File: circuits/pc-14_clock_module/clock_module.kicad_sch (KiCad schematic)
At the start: 7 parts, among them U1 74HCT74, U2 4011

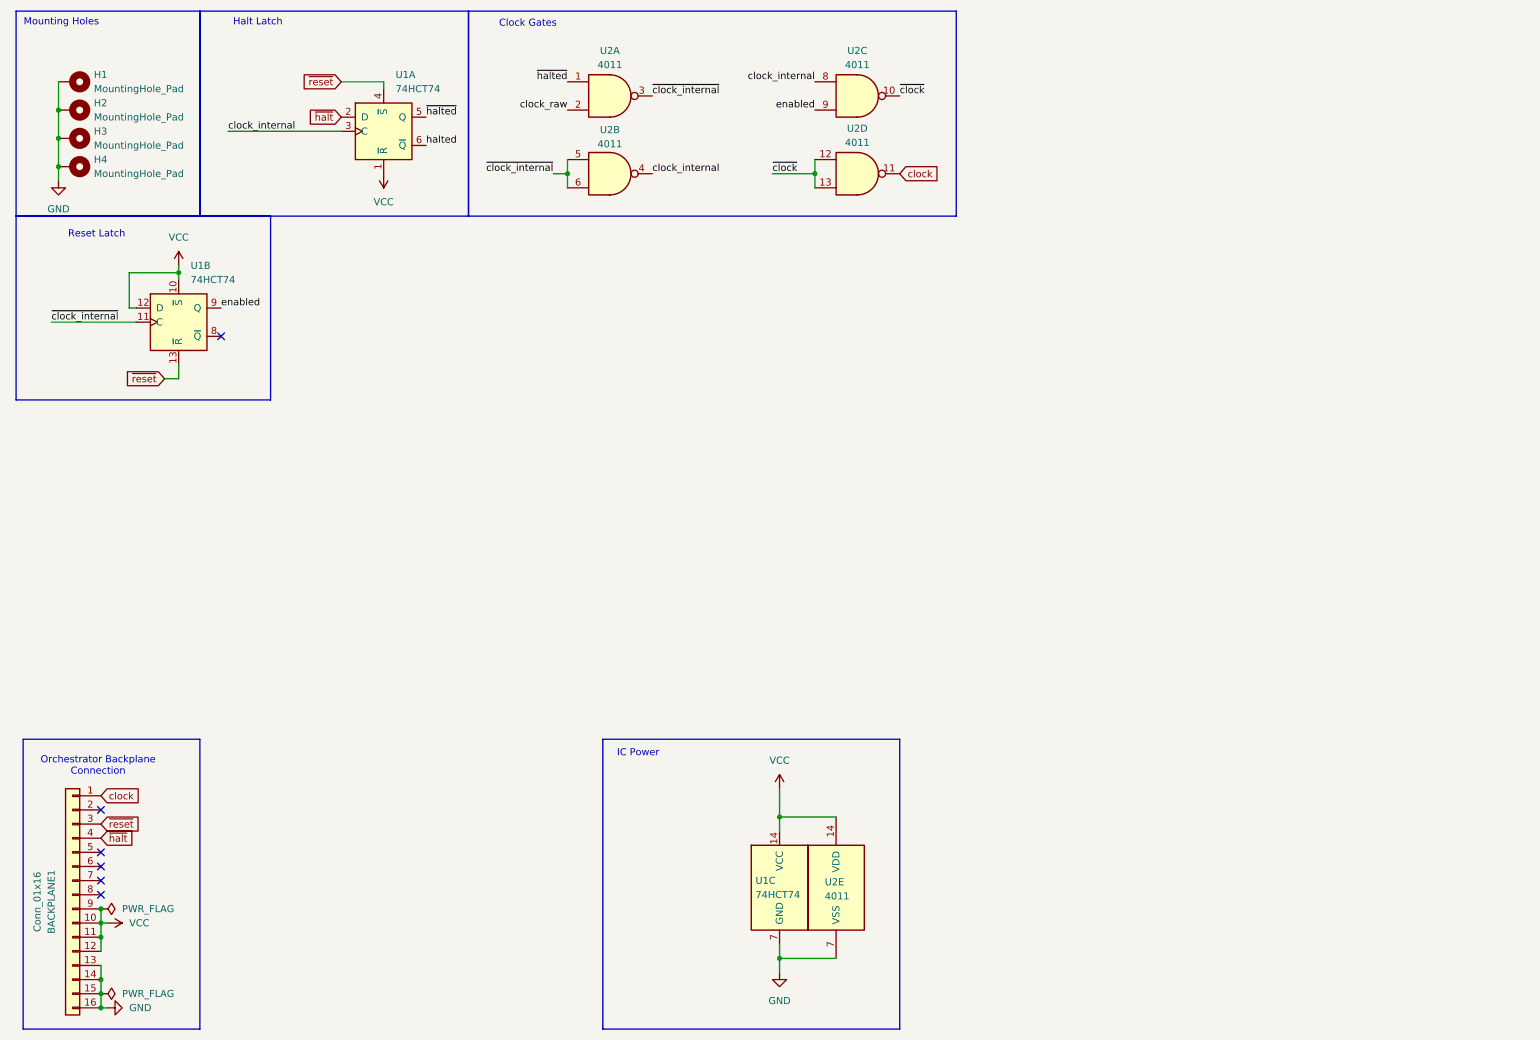
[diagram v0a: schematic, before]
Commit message: pc-14: continue clock module: full functionality and power-on reset logic.
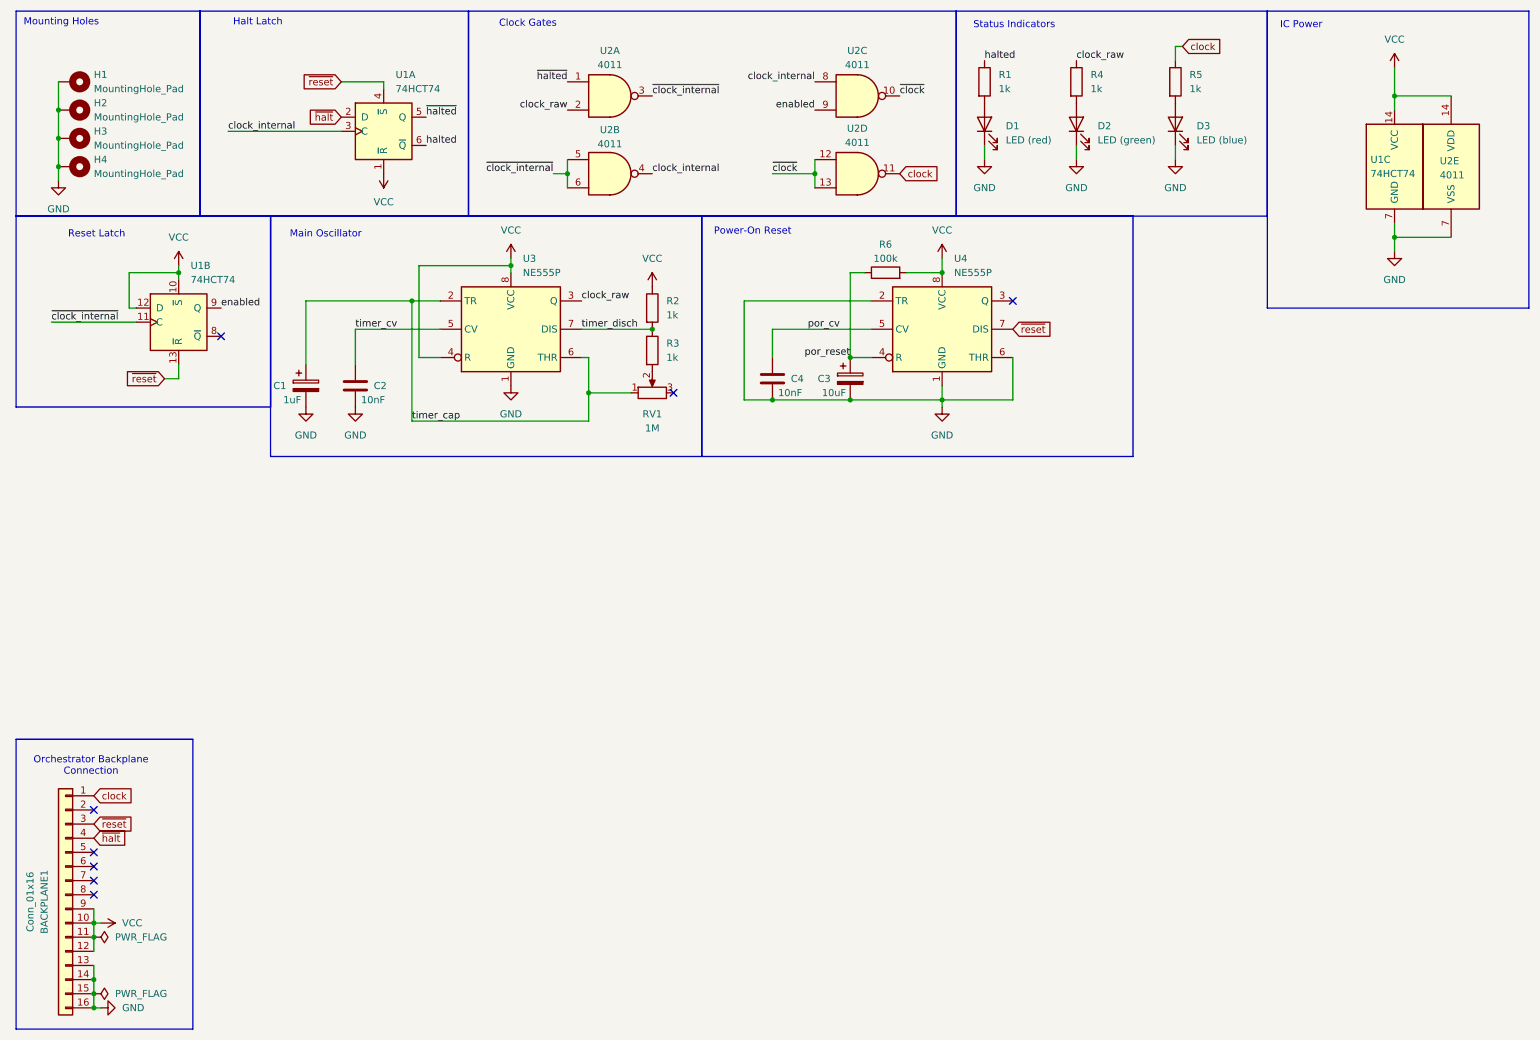
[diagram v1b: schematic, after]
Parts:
- added C1: 1uF, symbol Device:C_Polarized
- added C2, C4: 10nF, Capacitor_SMD:C_0603_1608Metric, symbol Device:C
- added C3: 10uF, symbol Device:C_Polarized
- added D1: LED (red), LED_SMD:LED_0603_1608Metric, symbol Device:LED
- added D2: LED (green), LED_SMD:LED_0603_1608Metric, symbol Device:LED
- added D3: LED (blue), LED_SMD:LED_0603_1608Metric, symbol Device:LED
- added R1, R2, R3, R4, R5: 1k, Resistor_SMD:R_0603_1608Metric, symbol Device:R
- added R6: 100k, Resistor_SMD:R_0603_1608Metric, symbol Device:R
- added RV1: 1M, symbol Device:R_Potentiometer
- added U3, U4: NE555P, Package_DIP:DIP-8_W7.62mm, symbol Timer:NE555P
- U1, U2: footprint (none) -> Package_DIP:DIP-14_W7.62mm
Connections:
- net GND: now also C1.2, C2.2, C3.2, C4.2, D1.1 (K), D2.1 (K), D3.1 (K), U3.1 (GND), U4.1 (GND), U4.2 (TR), U4.6 (THR)
- net VCC: now also R2.1, R6.2, U3.4 (R), U3.8 (VCC), U4.8 (VCC)
- net clock: now also R5.1
- net clock_raw: now also R4.1, U3.3 (Q)
- net halted: now also R1.1
- net ~{reset}: now also U4.7 (DIS)
- new net: D1.2 (A), R1.2
- new net: D2.2 (A), R4.2
- new net: D3.2 (A), R5.2
- new net: R3.2, RV1.2
- new net por_cv: C4.1, U4.5 (CV)
- new net por_reset: C3.1, R6.1, U4.4 (R)
- new net timer_cap: C1.1, RV1.1, U3.2 (TR), U3.6 (THR)
- new net timer_cv: C2.1, U3.5 (CV)
- new net timer_disch: R2.2, R3.1, U3.7 (DIS)
- no-connect marks 6 -> 8
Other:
- note added: "Main Oscillator"
- note added: "Power-On Reset"
- note added: "Status Indicators"
- moved on the sheet: BACKPLANE1, U1C, U2E
